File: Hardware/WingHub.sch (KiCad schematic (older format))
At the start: 11 parts, among them J1 Conn_Battery, J2 USB_A, J3 USB_A, J4 USB_B_Micro, J5 Conn_Left, J6 Conn_Right, SW1 RESET, SW2 DOWLOADER, U1 CH559L

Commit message: Update Wings format
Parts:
- removed J1: Conn_Battery, Connector_JST:JST_PH_B2B-PH-SM4-TB_1x02-1MP_P2.00mm_Vertical, symbol Connector_Generic:Conn_02x01
- removed J2: USB_A, Connector_USB:USB_A_CONNFLY_DS1095-WNR0, symbol Connector:USB_A
- removed J4: USB_B_Micro, Connector_USB:USB_Micro-B_Molex-105017-0001, symbol Connector:USB_B_Micro
- removed J5: Conn_Left, Connector_PinSocket_2.54mm:PinSocket_1x16_P2.54mm_Vertical, symbol Connector_Generic:Conn_01x16
- removed J6: Conn_Right, Connector_PinSocket_2.54mm:PinSocket_1x12_P2.54mm_Vertical, symbol Connector_Generic:Conn_01x12
- added J1: feather long, Connector_PinHeader_2.54mm:PinHeader_1x16_P2.54mm_Vertical, symbol Connector_Generic:Conn_01x16
- added J2: feather short, Connector_PinHeader_2.54mm:PinHeader_1x12_P2.54mm_Vertical, symbol Connector_Generic:Conn_01x12
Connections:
- net labels added: AREF, F0, F1, F2, F3, F4, F5, F6, FREE, VBAT, VUSB, ~RST
- wire segments 75 -> 104
- no-connect marks 2 -> 1
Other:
- moved on the sheet: C1, C2

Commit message: Update schematic
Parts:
- U1: symbol Electronic_Cats:CH559L -> WingHub-rescue:CH559L-Electronic_Cats
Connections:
- wire segments 104 -> 101
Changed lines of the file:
@@
 $EndDescr
 $Comp
-L Electronic_Cats:CH559L U1
+L WingHub-rescue:CH559L-Electronic_Cats U1
 U 1 1 5EC584A6
 P 4925 5525
@@
 $EndComp
 NoConn ~ 1700 4740
-Wire Wire Line
-	1775 6065 1775 6095
-Wire Wire Line
-	2075 5765 2165 5765
-Wire Wire Line
-	2075 5665 2160 5665
 Wire Wire Line
 	3775 4675 3705 4675
@@
 	1    0    0    -1
 $EndComp
+Wire Wire Line
+	9255 865  9255 965
+Wire Wire Line
+	9255 965  9605 965
+Wire Wire Line
+	9255 1265 9255 1165
+Wire Wire Line
+	9255 1165 9605 1165
+Wire Notes Line
+	9055 2515 11205 2515
+Wire Notes Line
+	9055 465  9055 2515
 $Comp
 L power:GND #PWR0102
@@
 	1    0    0    -1
 $EndComp
-Wire Wire Line
-	9255 865  9255 965
-Wire Wire Line
-	9255 965  9605 965
-Wire Wire Line
-	9255 1265 9255 1165
-Wire Wire Line
-	9255 1165 9605 1165
-Wire Notes Line
-	9055 465  9055 2515
-Wire Notes Line
-	9055 2515 11205 2515
 $EndSCHEMATC

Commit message: CH559L Updated
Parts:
- removed U1: CH559L, Package_QFP:LQFP-48_7x7mm_P0.5mm, symbol WingHub-rescue:CH559L-Electronic_Cats
- added U1: CH559T-Electronic_Cats, Package_SO:SSOP-20_5.3x7.2mm_P0.65mm, symbol WingHub-rescue:CH559T-Electronic_Cats
- SW2: value DOWLOADER -> DOWNLOADER
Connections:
- net labels removed: +BATT, Aref, D2+, D2-, GPIO05, GPIO06, GPIO09, GPIO10, GPIO11, GPIO12, GPIO13, MISC, ~RST~
- wire segments 101 -> 69
- no-connect marks 1 -> 14
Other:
- moved on the sheet: J1, J2, J3

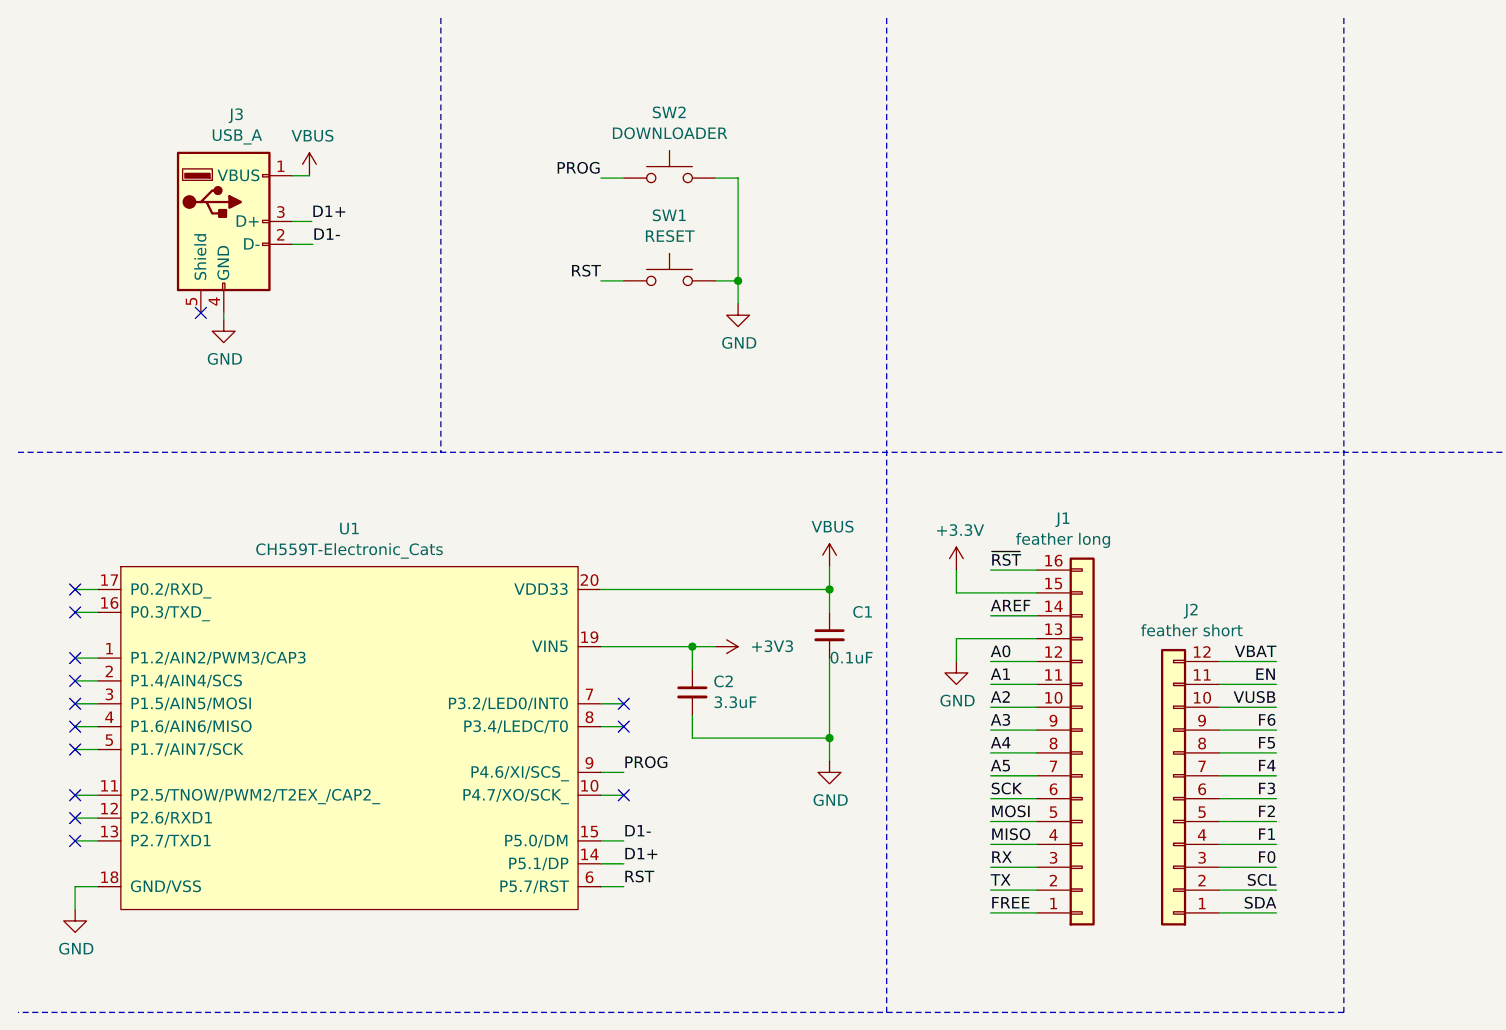
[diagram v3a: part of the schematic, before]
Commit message: Pre-routed HUSUSB PCB
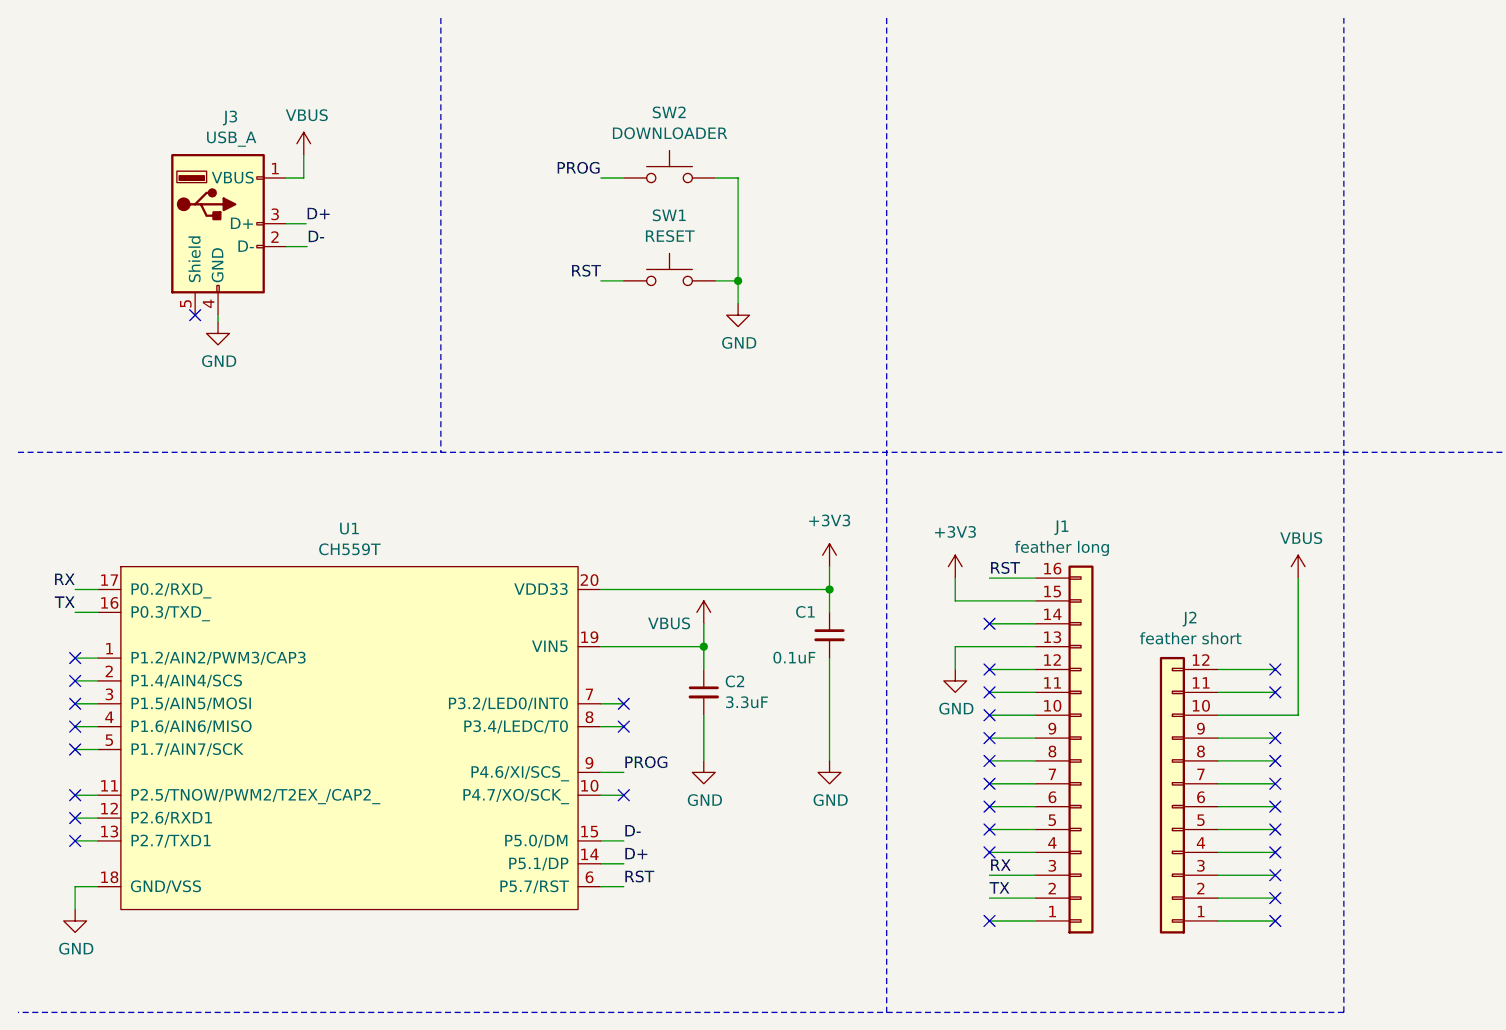
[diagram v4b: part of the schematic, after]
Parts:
- U1: value CH559T-Electronic_Cats -> CH559T
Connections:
- net VUSB is gone; now on net VBUS: J2.10 (Pin_10)
- net ~RST is gone; now on net RST: J1.16 (Pin_16)
- net +3V3: now also C1.1, U1.20 (VDD33); no longer C2.1, U1.19 (VIN5)
- net RX: now also U1.17 (P0.2/RXD_)
- net TX: now also U1.16 (P0.3/TXD_)
- net VBUS: now also C2.1, U1.19 (VIN5); no longer C1.1, U1.20 (VDD33)
- net A0: no longer names the net of J1.12 (Pin_12)
- net A1: no longer names the net of J1.11 (Pin_11)
- net A2: no longer names the net of J1.10 (Pin_10)
- net A3: no longer names the net of J1.9 (Pin_9)
- net A4: no longer names the net of J1.8 (Pin_8)
- net A5: no longer names the net of J1.7 (Pin_7)
- net AREF: no longer names the net of J1.14 (Pin_14)
- net D1+ renamed D+
- net D1- renamed D-
- net EN: no longer names the net of J2.11 (Pin_11)
- net F0: no longer names the net of J2.3 (Pin_3)
- net F1: no longer names the net of J2.4 (Pin_4)
- net F2: no longer names the net of J2.5 (Pin_5)
- net F3: no longer names the net of J2.6 (Pin_6)
- net F4: no longer names the net of J2.7 (Pin_7)
- net F5: no longer names the net of J2.8 (Pin_8)
- net F6: no longer names the net of J2.9 (Pin_9)
- net FREE: no longer names the net of J1.1 (Pin_1)
- net MISO: no longer names the net of J1.4 (Pin_4)
- net MOSI: no longer names the net of J1.5 (Pin_5)
- net SCK: no longer names the net of J1.6 (Pin_6)
- net SCL: no longer names the net of J2.2 (Pin_2)
- net SDA: no longer names the net of J2.1 (Pin_1)
- net VBAT: no longer names the net of J2.12 (Pin_12)
- no-connect marks 14 -> 34
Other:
- moved on the sheet: C2, J1, J2, J3

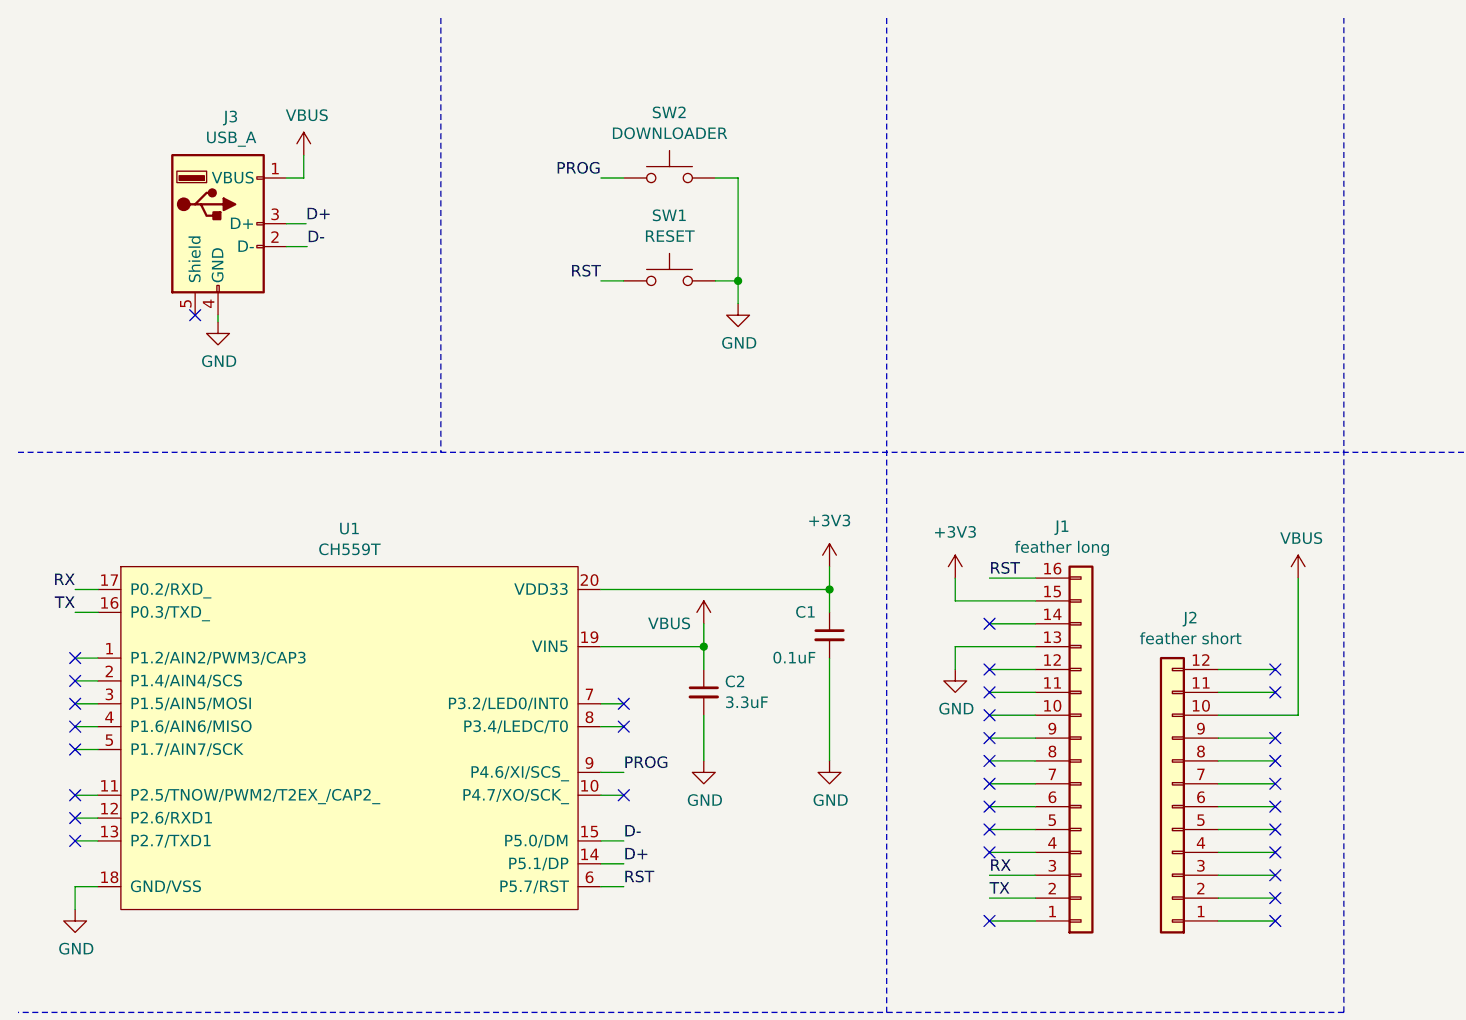
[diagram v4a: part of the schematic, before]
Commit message: add SPI and LED serial data
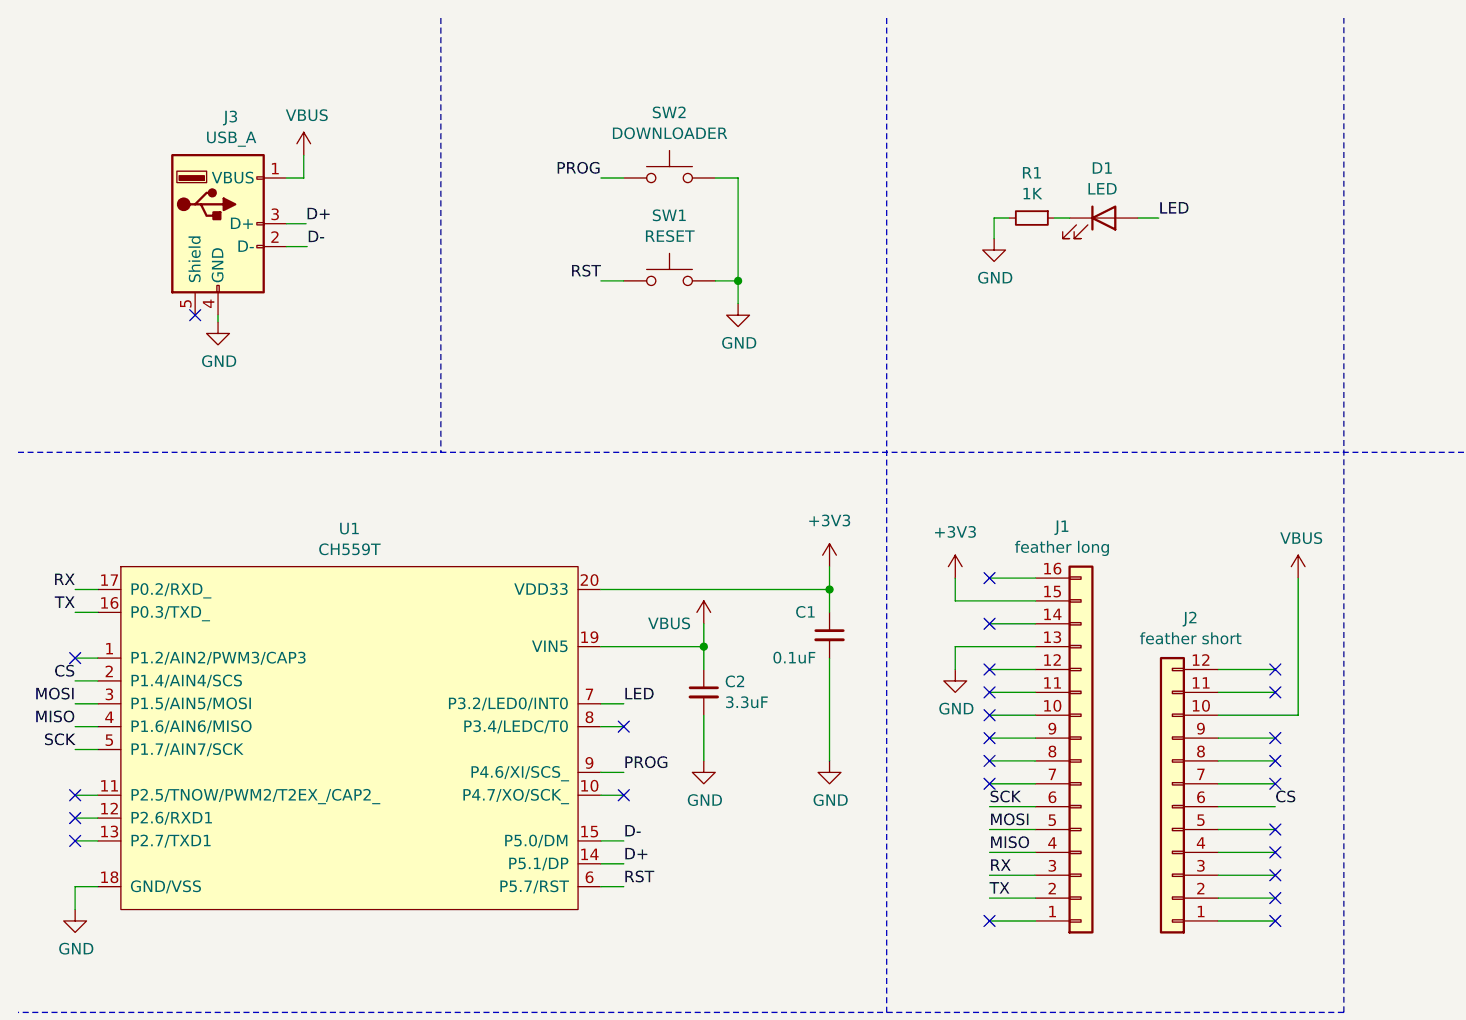
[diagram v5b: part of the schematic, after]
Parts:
- added D1: LED, LED_SMD:LED_0805_2012Metric, symbol Device:LED
- added R1: 1K, Resistor_SMD:R_0805_2012Metric, symbol Device:R_Small
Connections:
- net GND: now also R1.2
- net RST: no longer J1.16 (Pin_16)
- net MISO: now reaches J1.4 (Pin_4)
- net MISO: now also U1.4 (P1.6/AIN6/MISO)
- net MOSI: now reaches J1.5 (Pin_5)
- net MOSI: now also U1.3 (P1.5/AIN5/MOSI)
- net SCK: now reaches J1.6 (Pin_6)
- net SCK: now also U1.5 (P1.7/AIN7/SCK)
- net CS: now reaches J2.6 (Pin_6)
- net CS: now also U1.2 (P1.4/AIN4/SCS)
- net LED: now reaches U1.7 (P3.2/LED0/INT0)
- net LED: now also D1.2 (A)
- new net: D1.1 (K), R1.1
- no-connect marks 34 -> 26
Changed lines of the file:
@@
 NoConn ~ 3150 3900
 NoConn ~ 3150 3600
-NoConn ~ 3150 3500
 NoConn ~ 750  3300
-NoConn ~ 750  3400
-NoConn ~ 750  3500
-NoConn ~ 750  3600
-NoConn ~ 750  3700
 NoConn ~ 750  3900
 NoConn ~ 750  4000
@@
 	-1   0    0    1
 $EndComp
-Text Label 4750 2950 0    50   ~ 0
-RST
 Text Label 4750 4350 0    50   ~ 0
 TX
@@
 NoConn ~ 4750 3650
 NoConn ~ 4750 3750
-NoConn ~ 4750 3850
-NoConn ~ 4750 3950
-NoConn ~ 4750 4050
-NoConn ~ 4750 4150
 NoConn ~ 4750 4450
 NoConn ~ 6000 3350
@@
 NoConn ~ 6000 3750
 NoConn ~ 6000 3850
-NoConn ~ 6000 3950
 NoConn ~ 6000 4050
 NoConn ~ 6000 4150
@@
 Text Label 750  3100 2    50   ~ 0
 TX
+NoConn ~ 4750 2950
+Text Label 750  3700 2    50   ~ 0
+SCK
+Text Label 750  3600 2    50   ~ 0
+MISO
+Text Label 750  3500 2    50   ~ 0
+MOSI
+Text Label 750  3400 2    50   ~ 0
+CS
+$Comp
+L Device:LED D1
+U 1 1 5ED2458B
+P 5250 1375
+F 0 "D1" H 5243 1592 50  0000 C CNN
+F 1 "LED" H 5243 1501 50  0000 C CNN
+F 2 "LED_SMD:LED_0805_2012Metric" H 5250 1375 50  0001 C CNN
+F 3 "~" H 5250 1375 50  0001 C CNN
+	1    5250 1375
+	1    0    0    -1
+$EndComp
+$Comp
+L Device:R_Small R1
+U 1 1 5ED254AD
+P 4935 1375
+F 0 "R1" V 4739 1375 50  0000 C CNN
+F 1 "1K" V 4830 1375 50  0000 C CNN
+F 2 "Resistor_SMD:R_0805_2012Metric" H 4935 1375 50  0001 C CNN
+F 3 "~" H 4935 1375 50  0001 C CNN
+	1    4935 1375
+	0    1    1    0
+$EndComp
+Wire Wire Line
+	5100 1375 5035 1375
+Wire Wire Line
+	4835 1375 4770 1375
+Wire Wire Line
+	4770 1375 4770 1465
+Wire Wire Line
+	5400 1375 5490 1375
+Text Label 5490 1375 0    50   ~ 0
+LED
+$Comp
+L power:GND #PWR01
+U 1 1 5ED2B769
+P 4770 1465
+F 0 "#PWR01" H 4770 1215 50  0001 C CNN
+F 1 "GND" H 4775 1292 50  0000 C CNN
+F 2 "" H 4770 1465 50  0001 C CNN
+F 3 "" H 4770 1465 50  0001 C CNN
+	1    4770 1465
+	1    0    0    -1
+$EndComp
+Text Label 3150 3500 0    50   ~ 0
+LED
+Text Label 4750 4150 0    50   ~ 0
+MISO
+Text Label 4750 4050 0    50   ~ 0
+MOSI
+Text Label 4750 3950 0    50   ~ 0
+SCK
+NoConn ~ 4750 3850
+Text Label 6000 3950 0    50   ~ 0
+CS
 $EndSCHEMATC
